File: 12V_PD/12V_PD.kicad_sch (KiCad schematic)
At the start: 36 parts, among them IC1 TJA1044BT/0Z, J1 Conn_02x02_Top_Bottom, J11 39-28-1023, J12 39-28-1023, J14 39-28-1023, J15 39-28-1023, J16 39-28-1023, J17 39-28-1023, J18 39-28-1023, J19 39-28-1023, J2 39-28-1023, J20 39-28-1023, J3 Conn_02x02_Top_Bottom, J4 39-28-1023, J7 39-28-1023, J8 39-28-1023, J9 39-28-1023, M3 MountingHole, M3_1 MountingHole, M3_2 MountingHole, SW1 SML-S13UTT68, U2 ESP32-DEVKIT-C

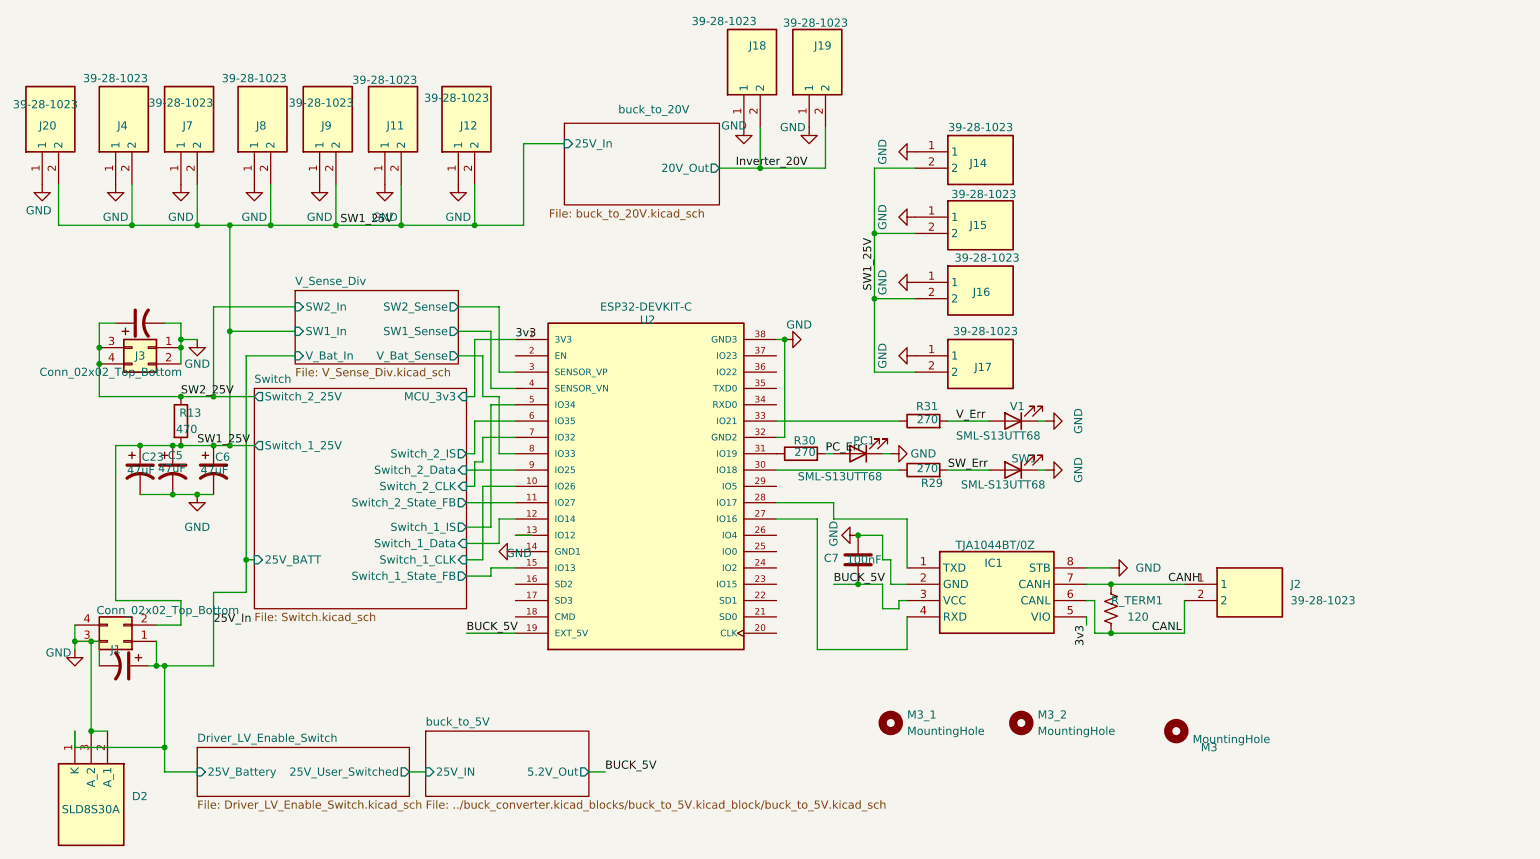
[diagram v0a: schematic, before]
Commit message: sry forgot to push, waiting on PCB shipping atm. Notes: split power distribution into two boards, one for the main 25V distribution, and another for 12V stuff. Also updated CAN transciever. the previous one was a 5V logic one (same logic as its power), and would have fried our ESPs data pins
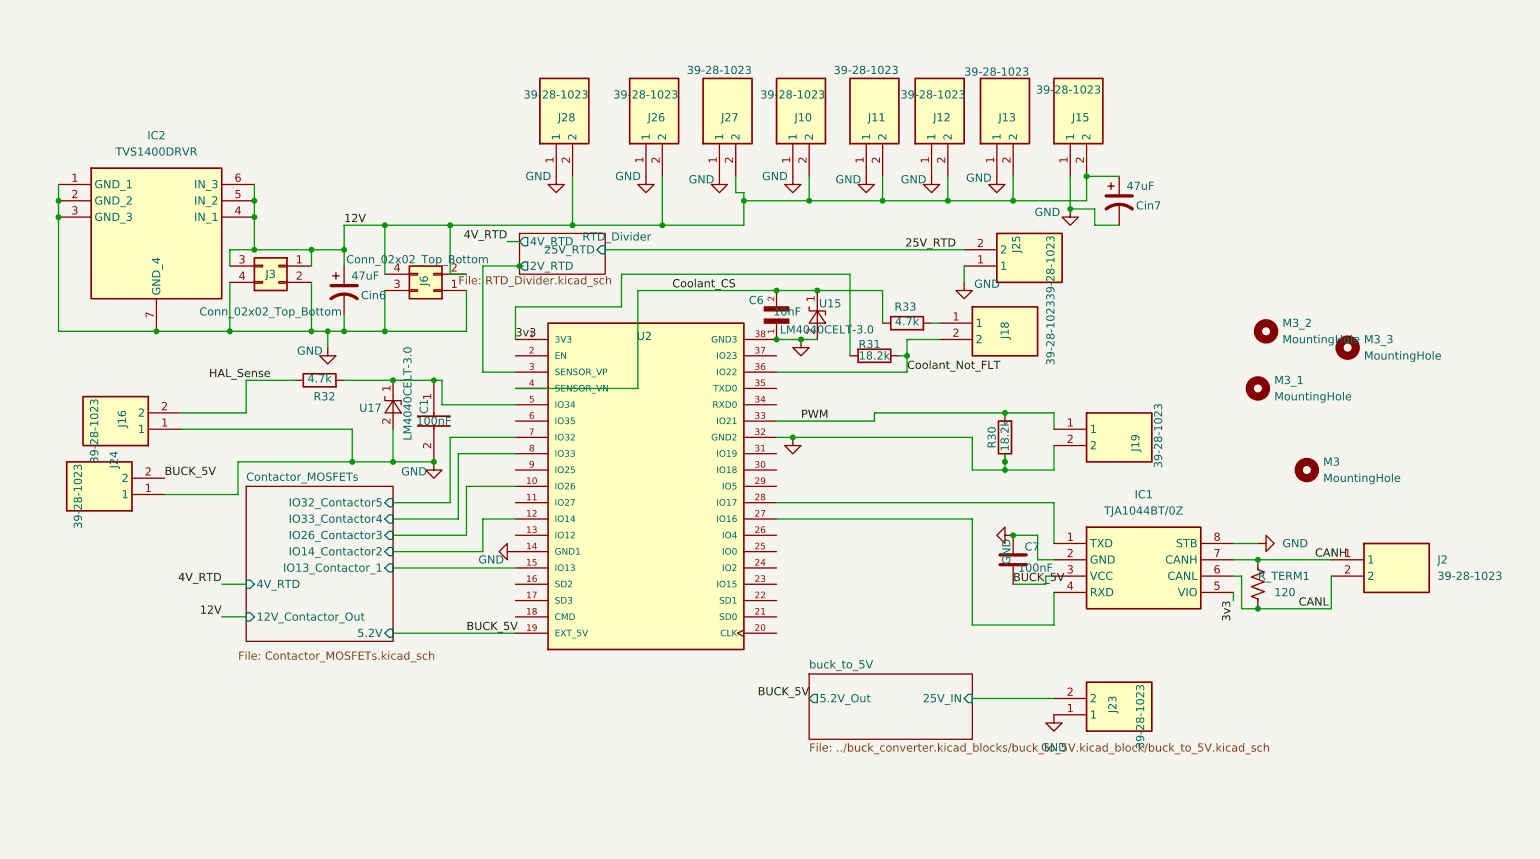
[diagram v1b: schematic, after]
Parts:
- removed C23, C5, C6: 47uF, Capacitor_SMD:CP_Elec_6.3x7.7, symbol Device:C_Polarized_US
- removed D2: SLD8S30A, PROVE-footprints:SLD8S30A, symbol PROVE_Symbols:SLD8S30A
- removed J1: Conn_02x02_Top_Bottom, PROVE-footprints:Anderson_PP1545_45A_2b2, symbol Connector_Generic:Conn_02x02_Top_Bottom
- removed J14, J17, J20, J4, J7, J8, J9: 39-28-1023, PROVE-footprints:39-28-1023, symbol PROVE_Symbols:39-28-1023
- removed PC1, SW1, V1: SML-S13UTT68, LED_SMD:LED_1206_3216Metric_Pad1.42x1.75mm_HandSolder, symbol Device:LED
- removed R13: 470, Resistor_SMD:R_2512_6332Metric_Pad1.40x3.35mm_HandSolder, symbol Device:R
- removed R29: 270, Resistor_SMD:R_0805_2012Metric_Pad1.20x1.40mm_HandSolder, symbol Device:R
- added C1: 100nF, Capacitor_SMD:C_0805_2012Metric_Pad1.18x1.45mm_HandSolder, symbol 08053C104KAT2A:08053C104KAT2A
- added C6: 10nF, Capacitor_SMD:C_0805_2012Metric_Pad1.18x1.45mm_HandSolder, symbol C0805C122J5GACTU:C0805C122J5GACTU
- added IC2: TVS1400DRVR, PROVE-footprints:SON65P200X200X80-7N, symbol PROVE_Symbols:TVS1400DRVR
- added J10, J13, J23, J24, J25, J26, J27, J28: 39-28-1023, PROVE-footprints:39-28-1023, symbol PROVE_Symbols:39-28-1023
- added J6: Conn_02x02_Top_Bottom, PROVE-footprints:Anderson_PP1545_45A_2b2, symbol Connector_Generic:Conn_02x02_Top_Bottom
- added M3_3: MountingHole, MountingHole:MountingHole_3.2mm_M3, symbol Mechanical:MountingHole
- added R32, R33: 4.7k, Resistor_SMD:R_0805_2012Metric_Pad1.20x1.40mm_HandSolder, symbol Device:R
- added U15, U17: LM4040CELT-3.0, Package_TO_SOT_SMD:SOT-23, symbol Reference_Voltage:LM4040DBZ-3
- R30, R31: value 270 -> 18.2k; Purchase Link https://www.mouser.com/en/ProductDetail/Vishay/CRCW0805270R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 -> https://www.mouser.com/en/ProductDetail/Vishay/CRCW080518K2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; Specs 270 Ω, ±1%, AEC-Q200 -> 18.2 kΩ, ±1%
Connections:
- net V_Err is gone; now on net 3v3: R31.2
- net BUCK_5V: now also J24.2
- net GND: now also J19.2, J3.4 (Pin_4), R30.1, C1.2, C6.1, IC2.1 (GND_1), IC2.2 (GND_2), IC2.3 (GND_3), IC2.7 (GND_4), J10.1, J13.1, J23.1, J24.1, J25.1, J26.1, J27.1, J28.1, J6.1 (Pin_1), J6.3 (Pin_3), U15.2 (A), U17.2 (A); no longer J18.1, J19.1, J3.1 (Pin_1)
- net at U2.31 (IO19): no longer R30.1
- net Coolant_Not_FLT: now reaches R31.1
- net Coolant_Not_FLT: now also J18.2, U2.36 (IO22); no longer U2.33 (IO21)
- net 25V_In renamed 12V
- net 12V: now also Cin6.1, J11.2, J12.2, J15.2, J3.1 (Pin_1), J3.3 (Pin_3), IC2.4 (IN_1), IC2.5 (IN_2), IC2.6 (IN_3), J10.2, J13.2, J26.2, J27.2, J28.2, J6.2 (Pin_2), J6.4 (Pin_4)
- removed net Inverter_20V: J18.2, J19.2
- net PC_Err renamed PWM
- net PWM: now also J19.1, U2.33 (IO21)
- removed net SW1_25V: J11.2, J12.2, J15.2, J16.2
- removed net SW2_25V: Cin6.1, J3.3 (Pin_3), J3.4 (Pin_4)
- net Switch/Switch_1_CLK renamed Contactor_MOSFETs/IO26_Contactor3
- net Switch/Switch_1_Data renamed Contactor_MOSFETs/IO14_Contactor2
- net Switch/Switch_1_IS: no longer names the net of U2.5 (IO34)
- net Switch/Switch_1_IS: now also C1.1, R32.2, U17.1 (K)
- net Switch/Switch_1_State_FB renamed Contactor_MOSFETs/IO13_Contactor_1
- net Switch/Switch_2_CLK renamed Contactor_MOSFETs/IO32_Contactor5
- net Switch/Switch_2_Data: no longer names the net of U2.9 (IO25)
- net Switch/Switch_2_IS: no longer names the net of U2.6 (IO35)
- net Switch/Switch_2_State_FB: no longer names the net of U2.11 (IO27)
- net V_Sense_Div/SW1_Sense renamed Coolant_CS
- net Coolant_CS: now also C6.2, R33.1, U15.1 (K)
- net V_Sense_Div/SW2_Sense renamed RTD_Divider/2V_RTD
- net V_Sense_Div/V_Bat_Sense renamed Contactor_MOSFETs/IO33_Contactor4
- new net: J18.1, R33.2
- new net 25V_RTD: J25.2
- new net HAL_Sense: J16.2, R32.1
- new net buck_to_5V/25V_IN: J23.2
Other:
- removed sheet Driver_LV_Enable_Switch
- removed sheet Switch
- removed sheet V_Sense_Div
- removed sheet buck_to_20V
- added sheet Contactor_MOSFETs (Contactor_MOSFETs.kicad_sch)
- added sheet RTD_Divider (RTD_Divider.kicad_sch)
- moved on the sheet: C7, IC1, J3, M3, M3_1, R_TERM1
